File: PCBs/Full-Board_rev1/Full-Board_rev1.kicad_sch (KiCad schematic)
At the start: 18 parts, among them J10 Conn_01x11, J2 Conn_01x05, J3 Conn_01x05, J4 Conn_01x05, J5 Conn_01x05, J6 MotorWithEncoder_M2, J7 MotorWithEncoder_M1, J8 Conn_01x02, J9 Conn_01x02, Q2 ESP32-C6-WROOM-1

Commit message: Added current measurement jumper
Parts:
- added J11: Conn_01x02_Pin, symbol Connector:Conn_01x02_Pin
- R8: value R -> 330
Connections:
- net 3V3: now also J11.1 (Pin_1)
- new net 3v3_Regulator/V_OUT: J11.2 (Pin_2)
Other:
- moved on the sheet: D1, R8
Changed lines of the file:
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@@
 	(text "IR Sensor Array"
 		(exclude_from_sim no)
-		(at 242.316 82.804 0)
+		(at 240.03 81.28 0)
 		(effects
 			(font
@@
 	)
 	(junction
-		(at 66.04 57.15)
+		(at 69.85 57.15)
 		(diameter 0)
 		(color 0 0 0 0)
@@
 	(wire
 		(pts
-			(xy 66.04 57.15) (xy 85.09 57.15)
+			(xy 69.85 57.15) (xy 85.09 57.15)
 		)
 		(stroke
@@
 	(wire
 		(pts
-			(xy 66.04 68.58) (xy 71.12 68.58)
+			(xy 69.85 68.58) (xy 73.66 68.58)
 		)
 		(stroke
@@
 	(wire
 		(pts
-			(xy 66.04 57.15) (xy 66.04 58.42)
+			(xy 69.85 57.15) (xy 69.85 58.42)
 		)
 		(stroke
@@
 	(wire
 		(pts
-			(xy 53.34 57.15) (xy 66.04 57.15)
-		)
-		(stroke
-			(width 0)
-			(type default)
-		)
-	)
-	(wire
-		(pts
 			(xy 66.04 168.91) (xy 67.31 168.91)
 		)
@@
 	(wire
 		(pts
-			(xy 78.74 68.58) (xy 78.74 72.39)
+			(xy 81.28 68.58) (xy 81.28 72.39)
 		)
 		(stroke
@@
 	(wire
 		(pts
+			(xy 63.5 57.15) (xy 69.85 57.15)
+		)
+		(stroke
+			(width 0)
+			(type default)
+		)
+	)
+	(wire
+		(pts
 			(xy 147.32 132.08) (xy 147.32 133.35)
 		)
@@
 	(wire
 		(pts
-			(xy 66.04 66.04) (xy 66.04 68.58)
+			(xy 69.85 66.04) (xy 69.85 68.58)
+		)
+		(stroke
+			(width 0)
+			(type default)
+		)
+	)
+	(wire
+		(pts
+			(xy 53.34 57.15) (xy 60.96 57.15)
 		)
 		(stroke
@@
 	(symbol
 		(lib_id "Device:R_US")
-		(at 66.04 62.23 0)
+		(at 69.85 62.23 0)
 		(unit 1)
 		(exclude_from_sim no)
@@
 		(fields_autoplaced yes)
 		(property "Reference" "R8"
-			(at 68.58 60.9599 0)
+			(at 72.39 60.9599 0)
 			(effects
 				(font
@@
 			)
 		)
-		(property "Value" "R"
-			(at 68.58 63.4999 0)
+		(property "Value" "330"
+			(at 72.39 63.4999 0)
 			(effects
 				(font
@@
 		)
 		(property "Footprint" ""
-			(at 67.056 62.484 90)
+			(at 70.866 62.484 90)
 			(effects
 				(font
@@
 		)
 		(property "Datasheet" "~"
-			(at 66.04 62.23 0)
+			(at 69.85 62.23 0)
 			(effects
 				(font
@@
 		)
 		(property "Description" "Resistor, US symbol"
-			(at 66.04 62.23 0)
+			(at 69.85 62.23 0)
 			(effects
 				(font
@@
 	(symbol
 		(lib_id "power:GND")
-		(at 78.74 72.39 0)
+		(at 81.28 72.39 0)
 		(unit 1)
 		(exclude_from_sim no)
@@
 		(fields_autoplaced yes)
 		(property "Reference" "#PWR013"
-			(at 78.74 78.74 0)
+			(at 81.28 78.74 0)
 			(effects
 				(font
@@
 		)
 		(property "Value" "GND"
-			(at 78.74 77.47 0)
+			(at 81.28 77.47 0)
 			(effects
 				(font
@@
 		)
 		(property "Footprint" ""
-			(at 78.74 72.39 0)
+			(at 81.28 72.39 0)
 			(effects
 				(font
@@
 		)
 		(property "Datasheet" ""
-			(at 78.74 72.39 0)
+			(at 81.28 72.39 0)
 			(effects
 				(font
@@
 		)
 		(property "Description" "Power symbol creates a global label with name \"GND\" , ground"
-			(at 78.74 72.39 0)
+			(at 81.28 72.39 0)
 			(effects
 				(font
@@
 		(on_board yes)
 		(dnp no)
-		(fields_autoplaced yes)
 		(property "Reference" "J10"
-			(at 248.92 100.3299 0)
+			(at 246.38 83.82 0)
 			(effects
 				(font
@@
 		)
 		(property "Value" "Conn_01x11"
-			(at 248.92 102.8699 0)
+			(at 246.38 86.36 0)
 			(effects
 				(font
@@
 		(on_board yes)
 		(dnp no)
-		(fields_autoplaced yes)
 		(property "Reference" "J8"
-			(at 143.51 172.7199 0)
+			(at 140.97 177.8 0)
 			(effects
 				(font
@@
 		)
 		(property "Value" "Conn_01x02"
-			(at 143.51 175.2599 0)
+			(at 140.97 180.34 0)
 			(effects
 				(font
@@
 	)
 	(symbol
+		(lib_id "Connector:Conn_01x02_Pin")
+		(at 63.5 52.07 270)
+		(unit 1)
+		(exclude_from_sim no)
+		(in_bom yes)
+		(on_board yes)
+		(dnp no)
+		(fields_autoplaced yes)
+		(property "Reference" "J11"
+			(at 64.77 51.4349 90)
+			(effects
+				(font
+					(size 1.27 1.27)
+				)
+				(justify left)
+			)
+		)
+		(property "Value" "Conn_01x02_Pin"
+			(at 64.77 53.9749 90)
+			(effects
+				(font
+					(size 1.27 1.27)
+				)
+				(justify left)
+			)
+		)
+		(property "Footprint" ""
+			(at 63.5 52.07 0)
+			(effects
+				(font
+					(size 1.27 1.27)
+				)
+				(hide yes)
+			)
+		)
+		(property "Datasheet" "~"
+			(at 63.5 52.07 0)
+			(effects
+				(font
+					(size 1.27 1.27)
+				)
+				(hide yes)
+			)
+		)
+		(property "Description" "Generic connector, single row, 01x02, script generated"
+			(at 63.5 52.07 0)
+			(effects
+				(font
+					(size 1.27 1.27)
+				)
+				(hide yes)
+			)
+		)
+		(pin "2"
+		)
+		(pin "1"
+		)
+		(instances
+			(project ""
+				(path "/2dd686ed-aa28-474a-bf3c-628eebb4b373"
+					(reference "J11")
+					(unit 1)
+				)
+			)
+		)
+	)
+	(symbol
 		(lib_id "Device:C_Small")
 		(at 137.16 52.07 0)
@@
 		(on_board yes)
 		(dnp no)
-		(fields_autoplaced yes)
 		(property "Reference" "J9"
-			(at 114.3 172.7199 0)
+			(at 111.76 177.8 0)
 			(effects
 				(font
@@
 		)
 		(property "Value" "Conn_01x02"
-			(at 114.3 175.2599 0)
+			(at 111.76 180.34 0)
 			(effects
 				(font
@@
 	(symbol
 		(lib_id "Device:LED")
-		(at 74.93 68.58 180)
+		(at 77.47 68.58 180)
 		(unit 1)
 		(exclude_from_sim no)
@@
 		(on_board yes)
 		(dnp no)
-		(fields_autoplaced yes)
 		(property "Reference" "D1"
-			(at 76.5175 60.96 0)
+			(at 74.93 71.12 0)
 			(effects
 				(font
@@
 		)
 		(property "Value" "PWR LED"
-			(at 76.5175 63.5 0)
+			(at 74.93 73.66 0)
 			(effects
 				(font
@@
 		)
 		(property "Footprint" ""
-			(at 74.93 68.58 0)
+			(at 77.47 68.58 0)
 			(effects
 				(font
@@
 		)
 		(property "Datasheet" "~"
-			(at 74.93 68.58 0)
+			(at 77.47 68.58 0)
 			(effects
 				(font
@@
 		)
 		(property "Description" "Light emitting diode"
-			(at 74.93 68.58 0)
+			(at 77.47 68.58 0)
 			(effects
 				(font
@@
 		)
 		(property "Sim.Pins" "1=K 2=A"
-			(at 74.93 68.58 0)
+			(at 77.47 68.58 0)
 			(effects
 				(font

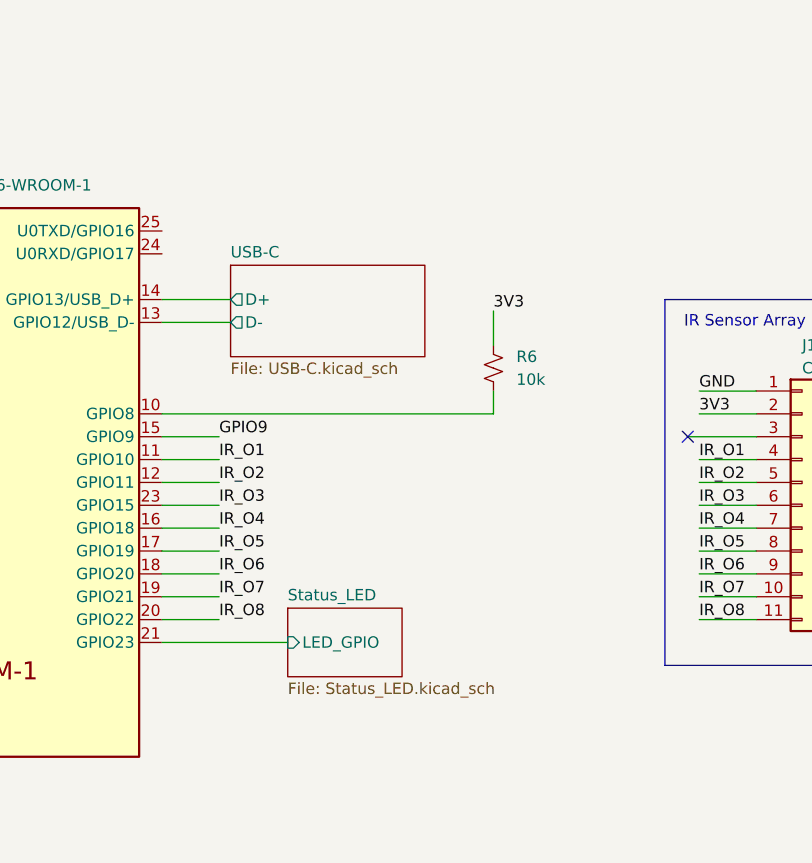
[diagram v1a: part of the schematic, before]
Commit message: Fixed some rules checker errors
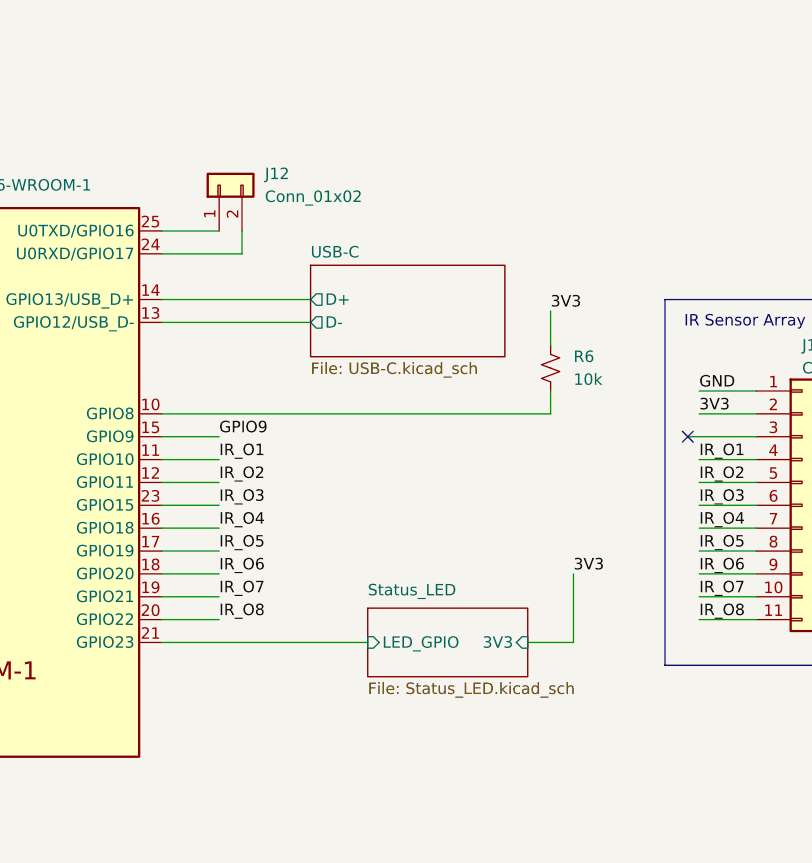
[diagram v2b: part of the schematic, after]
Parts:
- added J12: Conn_01x02, symbol Connector_Generic:Conn_01x02
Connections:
- net at Q2.24 (U0RXD/GPIO17): now also J12.2 (Pin_2)
- net at Q2.25 (U0TXD/GPIO16): now also J12.1 (Pin_1)
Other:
- sheet Status_LED ports: added 3V3; removed none
- moved on the sheet: R6
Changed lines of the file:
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@@
 	(wire
 		(pts
-			(xy 175.26 91.44) (xy 212.09 91.44)
+			(xy 175.26 91.44) (xy 218.44 91.44)
 		)
 		(stroke
@@
 	(wire
 		(pts
-			(xy 175.26 78.74) (xy 182.88 78.74)
+			(xy 175.26 78.74) (xy 191.77 78.74)
 		)
 		(stroke
@@
 	(wire
 		(pts
-			(xy 212.09 88.9) (xy 212.09 91.44)
+			(xy 218.44 88.9) (xy 218.44 91.44)
 		)
 		(stroke
@@
 	(wire
 		(pts
+			(xy 175.26 73.66) (xy 184.15 73.66)
+		)
+		(stroke
+			(width 0)
+			(type default)
+		)
+	)
+	(wire
+		(pts
 			(xy 63.5 57.15) (xy 69.85 57.15)
 		)
@@
 	(wire
 		(pts
-			(xy 175.26 116.84) (xy 189.23 116.84)
+			(xy 67.31 132.08) (xy 71.12 132.08)
 		)
 		(stroke
@@
 	(wire
 		(pts
-			(xy 67.31 132.08) (xy 71.12 132.08)
+			(xy 175.26 116.84) (xy 198.12 116.84)
 		)
 		(stroke
@@
 	(wire
 		(pts
-			(xy 182.88 81.28) (xy 175.26 81.28)
+			(xy 191.77 81.28) (xy 175.26 81.28)
 		)
 		(stroke
@@
 	(wire
 		(pts
+			(xy 175.26 71.12) (xy 181.61 71.12)
+		)
+		(stroke
+			(width 0)
+			(type default)
+		)
+	)
+	(wire
+		(pts
 			(xy 95.25 60.96) (xy 95.25 63.5)
 		)
@@
 	(wire
 		(pts
+			(xy 184.15 73.66) (xy 184.15 71.12)
+		)
+		(stroke
+			(width 0)
+			(type default)
+		)
+	)
+	(wire
+		(pts
 			(xy 127 54.61) (xy 127 58.42)
 		)
@@
 	(wire
 		(pts
-			(xy 212.09 80.01) (xy 212.09 83.82)
+			(xy 218.44 80.01) (xy 218.44 83.82)
 		)
 		(stroke
@@
 	(wire
 		(pts
+			(xy 215.9 116.84) (xy 220.98 116.84)
+		)
+		(stroke
+			(width 0)
+			(type default)
+		)
+	)
+	(wire
+		(pts
 			(xy 38.1 163.83) (xy 39.37 163.83)
 		)
@@
 	(wire
 		(pts
+			(xy 220.98 109.22) (xy 220.98 116.84)
+		)
+		(stroke
+			(width 0)
+			(type default)
+		)
+	)
+	(wire
+		(pts
 			(xy 66.04 161.29) (xy 67.31 161.29)
 		)
@@
 	)
 	(label "3V3"
+		(at 220.98 109.22 0)
+		(effects
+			(font
+				(size 1.27 1.27)
+			)
+			(justify left bottom)
+		)
+	)
+	(label "3V3"
 		(at 130.81 46.99 0)
 		(effects
@@
 	)
 	(label "3V3"
-		(at 212.09 80.01 0)
+		(at 218.44 80.01 0)
 		(effects
 			(font
@@
 	(symbol
 		(lib_id "Device:R_Small_US")
-		(at 212.09 86.36 0)
+		(at 218.44 86.36 0)
 		(unit 1)
 		(exclude_from_sim no)
@@
 		(fields_autoplaced yes)
 		(property "Reference" "R6"
-			(at 214.63 85.0899 0)
+			(at 220.98 85.0899 0)
 			(effects
 				(font
@@
 		)
 		(property "Value" "10k"
-			(at 214.63 87.6299 0)
+			(at 220.98 87.6299 0)
 			(effects
 				(font
@@
 		)
 		(property "Footprint" ""
-			(at 212.09 86.36 0)
+			(at 218.44 86.36 0)
 			(effects
 				(font
@@
 		)
 		(property "Datasheet" "~"
-			(at 212.09 86.36 0)
+			(at 218.44 86.36 0)
 			(effects
 				(font
@@
 		)
 		(property "Description" "Resistor, small US symbol"
-			(at 212.09 86.36 0)
+			(at 218.44 86.36 0)
 			(effects
 				(font
@@
 	)
 	(symbol
+		(lib_id "Connector_Generic:Conn_01x02")
+		(at 181.61 66.04 90)
+		(unit 1)
+		(exclude_from_sim no)
+		(in_bom yes)
+		(on_board yes)
+		(dnp no)
+		(fields_autoplaced yes)
+		(property "Reference" "J12"
+			(at 186.69 64.7699 90)
+			(effects
+				(font
+					(size 1.27 1.27)
+				)
+				(justify right)
+			)
+		)
+		(property "Value" "Conn_01x02"
+			(at 186.69 67.3099 90)
+			(effects
+				(font
+					(size 1.27 1.27)
+				)
+				(justify right)
+			)
+		)
+		(property "Footprint" ""
+			(at 181.61 66.04 0)
+			(effects
+				(font
+					(size 1.27 1.27)
+				)
+				(hide yes)
+			)
+		)
+		(property "Datasheet" "~"
+			(at 181.61 66.04 0)
+			(effects
+				(font
+					(size 1.27 1.27)
+				)
+				(hide yes)
+			)
+		)
+		(property "Description" "Generic connector, single row, 01x02, script generated (kicad-library-utils/schlib/autogen/connector/)"
+			(at 181.61 66.04 0)
+			(effects
+				(font
+					(size 1.27 1.27)
+				)
+				(hide yes)
+			)
+		)
+		(pin "1"
+		)
+		(pin "2"
+		)
+		(instances
+			(project "Full-Board_rev1"
+				(path "/2dd686ed-aa28-474a-bf3c-628eebb4b373"
+					(reference "J12")
+					(unit 1)
+				)
+			)
+		)
+	)
+	(symbol
 		(lib_id "Device:R_Small_US")
 		(at 95.25 66.04 0)
@@
 	)
 	(sheet
-		(at 182.88 74.93)
+		(at 191.77 74.93)
 		(size 21.59 10.16)
 		(exclude_from_sim no)
@@
 		)
 		(property "Sheetname" "USB-C"
-			(at 182.88 74.2184 0)
+			(at 191.77 74.2184 0)
 			(effects
 				(font
@@
 		)
 		(property "Sheetfile" "USB-C.kicad_sch"
-			(at 182.88 85.6746 0)
+			(at 191.77 85.6746 0)
 			(effects
 				(font
@@
 		)
 		(pin "D-" output
-			(at 182.88 81.28 180)
+			(at 191.77 81.28 180)
 			(effects
 				(font
@@
 		)
 		(pin "D+" output
-			(at 182.88 78.74 180)
+			(at 191.77 78.74 180)
 			(effects
 				(font
@@
 	)
 	(sheet
-		(at 189.23 113.03)
-		(size 12.7 7.62)
+		(at 198.12 113.03)
+		(size 17.78 7.62)
 		(exclude_from_sim no)
 		(in_bom yes)
 		(on_board yes)
 		(dnp no)
-		(fields_autoplaced yes)
 		(stroke
 			(width 0.1524)
@@
 		)
 		(property "Sheetname" "Status_LED"
-			(at 189.23 112.3184 0)
+			(at 198.12 111.76 0)
 			(effects
 				(font
@@
 		)
 		(property "Sheetfile" "Status_LED.kicad_sch"
-			(at 189.23 121.2346 0)
+			(at 198.12 121.2346 0)
 			(effects
 				(font
@@
 		)
 		(pin "LED_GPIO" input
-			(at 189.23 116.84 180)
+			(at 198.12 116.84 180)
 			(effects
 				(font
@@
 			)
 		)
+		(pin "3V3" input
+			(at 215.9 116.84 0)
+			(effects
+				(font
+					(size 1.27 1.27)
+				)
+				(justify right)
+			)
+		)
